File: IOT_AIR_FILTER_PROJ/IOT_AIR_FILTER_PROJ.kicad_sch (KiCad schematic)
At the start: 21 parts, among them J1 Conn_ARM_SWD_TagConnect_TC203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, J2 Conn_01x02_Socket, J3 Conn_01x04_Pin, J4 Conn_01x04_Pin, J5 Conn_01x04_Pin, J6 Conn_01x04_Pin, J7 Conn_01x04_Pin, U1 PIC16F18124-I/SL, U2 AMS1117-5.0, U3 ADG419BR

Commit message: minor changes to schematic, component selection and layout
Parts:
- removed C1: 22uF, Capacitor_SMD:C_1210_3225Metric, symbol Device:C
- added C1, C6: 47uF, Capacitor_SMD:CP_Elec_4x3, symbol Device:C_Polarized
- added R4, R5: 4.7k, Resistor_SMD:R_0805_2012Metric, symbol Device:R
- C2: value 22uF -> 100nF
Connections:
- net +12V: now also C1.1
- net +5V: now also C6.1, R4.1, R5.1
- net GND: now also C1.2, C6.2
- net at J3.3 (Pin_3), U3.2: now also R5.2
- net at J4.3 (Pin_3), U3.8: now also R4.2
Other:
- moved on the sheet: C2, J3, J4

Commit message: added schematics/layout/manufacturing files. Also initial FW for IOT sensor
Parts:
- removed C2: 100nF, Capacitor_SMD:C_1210_3225Metric, symbol Device:C
- removed U1: PIC16F18124-I/SL, PIC16F18124:PIC16F18124_SOIC14_SL_MCH, symbol PIC18F18124:PIC16F18124-I_SL
- added U4: PIC16F18124, Package_DIP:DIP-14_W7.62mm, symbol PIC16F18124_PDIP:PIC16F18124
- C1, C6: footprint Capacitor_SMD:CP_Elec_4x3 -> Capacitor_SMD:CP_Elec_6.3x5.4
- J3, J4: footprint Connector_PinHeader_2.54mm:PinHeader_1x04_P2.54mm_Horizontal -> Connector:FanPinHeader_1x04_P2.54mm_Vertical
- J5, J6, J7: footprint Connector_PinHeader_2.54mm:PinHeader_1x04_P2.54mm_Horizontal -> Connector_PinHeader_2.54mm:PinHeader_1x04_P2.54mm_Vertical
- R3: value 432 -> 470
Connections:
- net +5V: now also U4.1 (VDD)
- net FAN_TACH_SELECT: now also U4.11 (RA2)
- net GND: now also U4.14 (VSS); no longer J1.6 (SWO)
- net PWM11: now also U4.9 (RC1)
- net PWM12: now also U4.8 (RC2)
- net RST: now also U4.4 (RA3/*MCLR/VPP)
- net RX: now also J7.3 (Pin_3), U4.3 (RA4); no longer J7.4 (Pin_4)
- net SCL: now also U4.6 (RC4)
- net SDA: now also U4.7 (RC3)
- net SWCLK: now also U4.12 (RA1/ICSPCLK)
- net SWDIO: now also U4.13 (RA0/ICSPDAT)
- net T1CKI: now also U4.10 (RC0)
- net TX: now also J7.4 (Pin_4), U4.2 (RA5); no longer J7.3 (Pin_3)
- net at R3.1: now also U4.5 (RC5)
- no-connect marks 0 -> 1

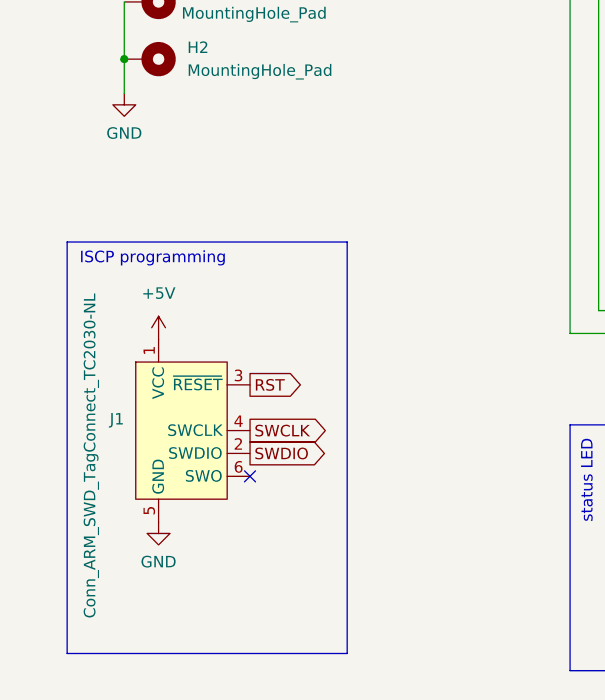
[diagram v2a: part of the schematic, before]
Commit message: added raspberry pi stuff
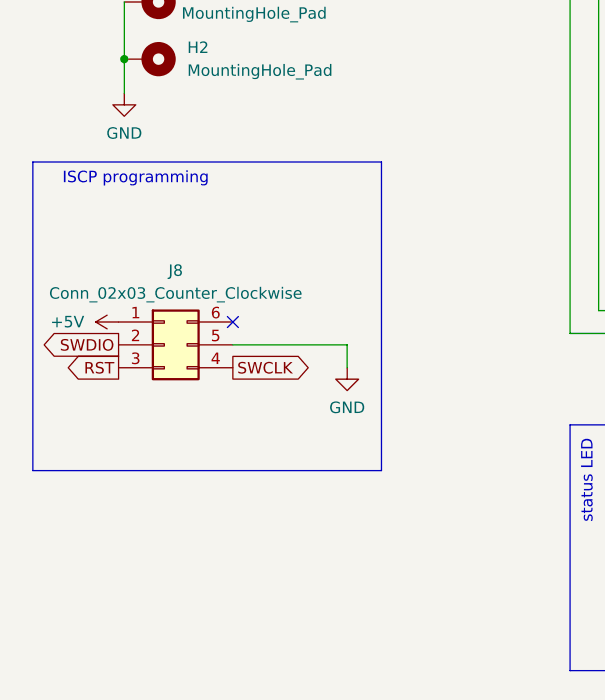
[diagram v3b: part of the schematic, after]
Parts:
- removed J1: Conn_ARM_SWD_TagConnect_TC2030-NL, Connector:Tag-Connect_TC2030-IDC-NL_2x03_P1.27mm_Vertical, symbol Connector:Conn_ARM_SWD_TagConnect_TC2030-NL
- added J8: Conn_02x03_Counter_Clockwise, Connector_PinSocket_2.54mm:PinSocket_2x03_P2.54mm_Vertical, symbol Connector_Generic:Conn_02x03_Counter_Clockwise
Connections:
- net +5V: now also J8.1 (Pin_1)
- net GND: now also J8.5 (Pin_5)
- net RST: now also J8.3 (Pin_3)
- net SWCLK: now also J8.4 (Pin_4)
- net SWDIO: now also J8.2 (Pin_2)
